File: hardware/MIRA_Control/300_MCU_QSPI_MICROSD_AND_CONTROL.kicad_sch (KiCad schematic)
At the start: 34 parts, among them J300 DM3AT-SF-PEJM5, U100 STM32H745IIT6, U300 W25Q512JVEIQ, U301 USBLC6-2SC6, U302 USBLC6-2SC6, U303 USBLC6-2SC6

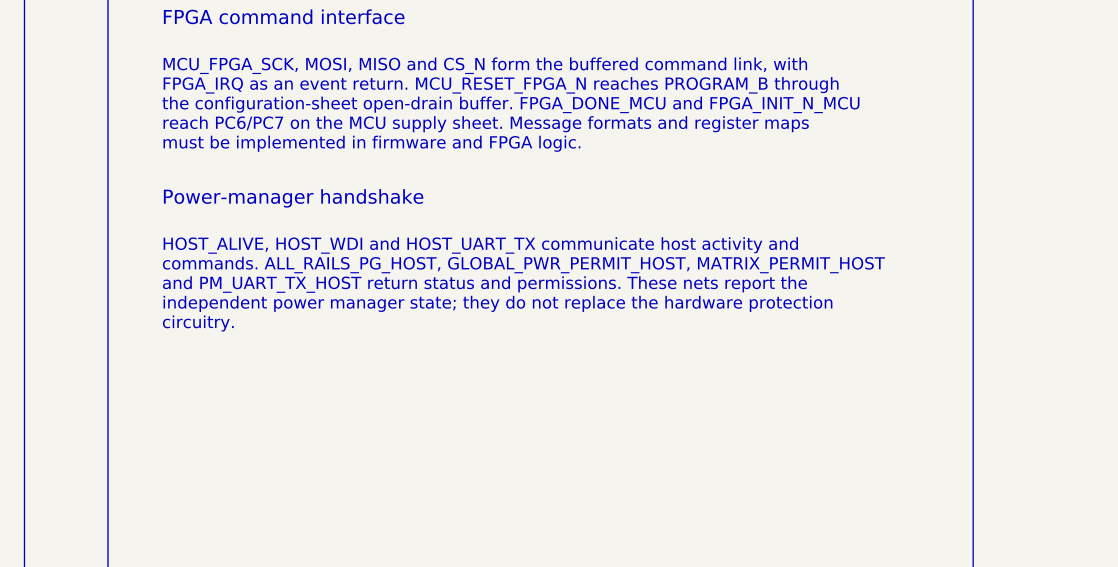
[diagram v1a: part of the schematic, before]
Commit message: Protect unpowered signal domains and qualify local supplies; retain startup and fault interlocks
MIRA-Startup-Patch: 7ffae17756ebcf923eff1212bb1aade8fbdfae03a9ca8ecebc69d3da3d3b4ba2
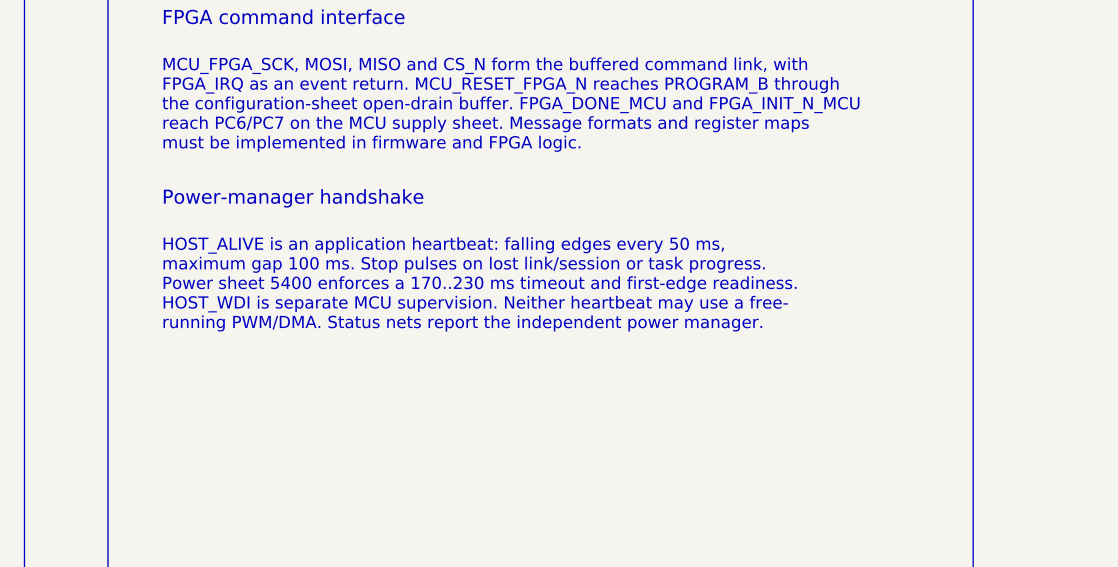
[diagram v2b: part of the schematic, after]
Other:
- note added: "HOST_ALIVE is an application heartbeat: falling edges every 50 ms, maximum gap 100 ms. Stop pulses on lost link/session or task progress. Power sheet 5400 enforces a 170..230 ms timeout and first-edge readiness. HOST_WDI is separate MCU supervision. Neither heartbeat may use a free- running PWM/DMA. Status nets report the independent power manager."
- note removed: "HOST_ALIVE, HOST_WDI and HOST_UART_TX communicate host activity and commands. ALL_RAILS_PG_HOST, GLOBAL_PWR_PERMIT_HOST, MATRIX_PERMIT_HOST and PM_UART_TX_HOST return status and permissions. These nets report the independent power manager state; they do not replace the hardware protection circuitry."
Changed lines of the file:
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@@
 		)
 	)
-	(text "HOST_ALIVE, HOST_WDI and HOST_UART_TX communicate host activity and\ncommands. ALL_RAILS_PG_HOST, GLOBAL_PWR_PERMIT_HOST, MATRIX_PERMIT_HOST\nand PM_UART_TX_HOST return status and permissions. These nets report the\nindependent power manager state; they do not replace the hardware protection\ncircuitry."
+	(text "HOST_ALIVE is an application heartbeat: falling edges every 50 ms,\nmaximum gap 100 ms. Stop pulses on lost link/session or task progress.\nPower sheet 5400 enforces a 170..230 ms timeout and first-edge readiness.\nHOST_WDI is separate MCU supervision. Neither heartbeat may use a free-\nrunning PWM/DMA. Status nets report the independent power manager."
 		(exclude_from_sim no)
 		(at 315 122.205 0)
